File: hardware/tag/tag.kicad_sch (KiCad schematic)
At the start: 119 parts, among them J1 USB_C_Receptacle_USB2.0_16P, J10 Conn_01x02, J2 BATTERY, J3 BLE_Conn, J4 SOURCE, J5 STM SWD, J6 I2C, J7 UART, J8 BLE SWD, J9 AUX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

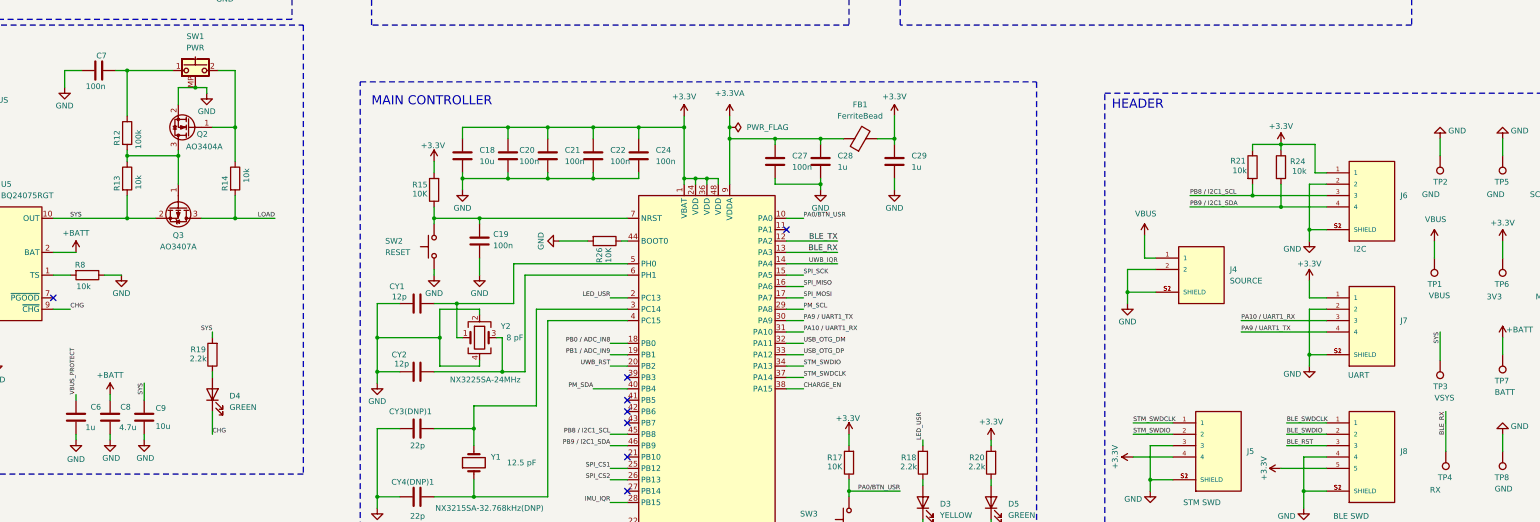
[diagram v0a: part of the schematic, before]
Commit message: update: add schottky diode to prevent the biased voltage back to soft latch circuit
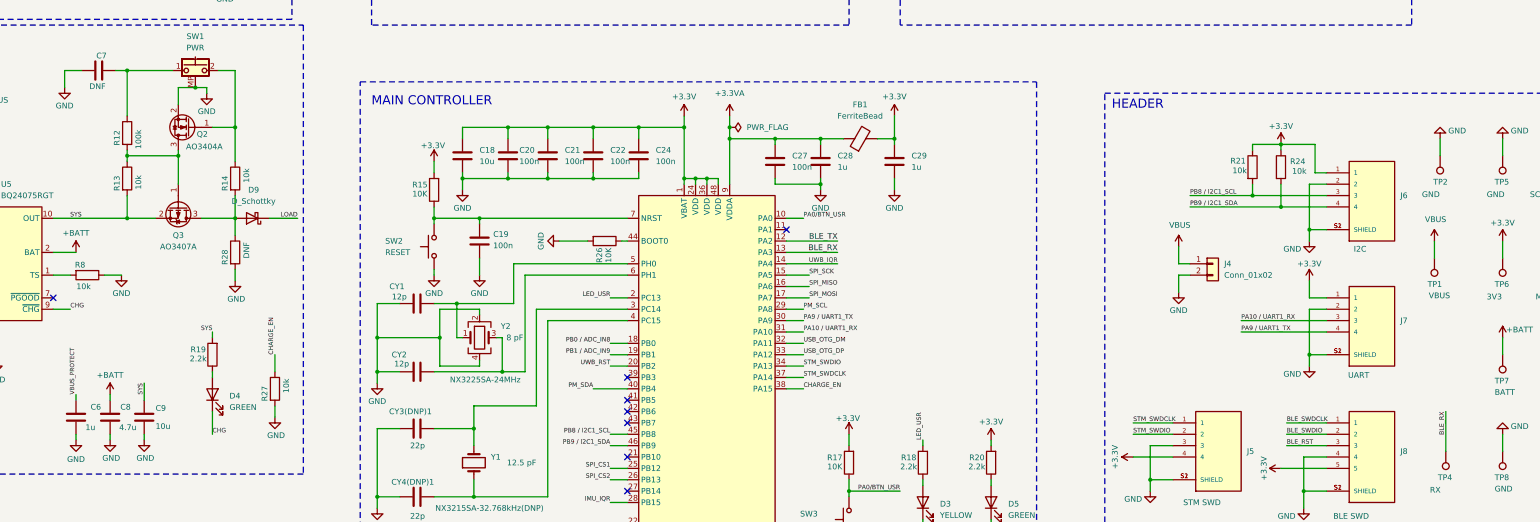
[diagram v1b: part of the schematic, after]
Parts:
- removed J4: SOURCE, Connector_JST:JST_PH_B2B-PH-K_1x02_P2.00mm_Vertical, symbol BM02B-SRSS-TB_LF__SN_:BM02B-SRSS-TB_LF__SN_
- removed TP3: VSYS, TestPoint:TestPoint_Pad_D1.5mm, symbol Connector:TestPoint
- added D9: D_Schottky, Diode_SMD:D_SOD-123, symbol Device:D_Schottky
- added J4: Conn_01x02, symbol Connector_Generic:Conn_01x02
- added R27: 10k, Resistor_SMD:R_0603_1608Metric, symbol Device:R
- added R28: DNF, Resistor_SMD:R_0603_1608Metric, symbol Device:R
- C1, C11, C12, C14, C2, C6, C8: footprint Capacitor_SMD:C_0805_2012Metric_Pad1.18x1.45mm_HandSolder -> Capacitor_SMD:C_0805_2012Metric
- C3, C4, C5: footprint Capacitor_SMD:C_0603_1608Metric_Pad1.08x0.95mm_HandSolder -> Capacitor_SMD:C_0603_1608Metric
- C7: value 100n -> DNF; footprint Capacitor_SMD:C_0603_1608Metric_Pad1.08x0.95mm_HandSolder -> Capacitor_SMD:C_0603_1608Metric
- R1, R11, R12, R13, R14, R19, R2, R5, R6, R8: footprint Resistor_SMD:R_0603_1608Metric_Pad0.98x0.95mm_HandSolder -> Resistor_SMD:R_0603_1608Metric
- TP10, TP11, TP12, TP13, TP14, TP15, TP4, TP9: footprint TestPoint:TestPoint_Pad_D1.5mm -> TestPoint:TestPoint_Pad_D1.0mm
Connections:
- net CHARGE_EN: now also R27.1
- net GND: now also J4.2 (Pin_2), R27.2, R28.2
- net LOAD: now also D9.1 (K); no longer Q3.3 (D), R14.2
- net VBUS: now also J4.1 (Pin_1)
- new net: D9.2 (A), Q3.3 (D), R14.2, R28.1

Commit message: wip hardware changes
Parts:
- C7: value DNF -> 100n(TBD)
- D8, D9: value D_Schottky -> MBR230LSFT1G
- J4: value Conn_01x02 -> EXT VBUS
- R28: value DNF -> 1k(TBD)
- R8: value 10k -> NTC 10k
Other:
- moved on the sheet: J4
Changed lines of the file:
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@@
 	(wire
 		(pts
-			(xy 360.68 185.42) (xy 358.14 185.42)
+			(xy 359.41 186.69) (xy 356.87 186.69)
 		)
 		(stroke
@@
 	(wire
 		(pts
-			(xy 358.14 187.96) (xy 358.14 191.77)
+			(xy 356.87 189.23) (xy 356.87 193.04)
 		)
 		(stroke
@@
 	(wire
 		(pts
-			(xy 360.68 187.96) (xy 358.14 187.96)
+			(xy 359.41 189.23) (xy 356.87 189.23)
 		)
 		(stroke
@@
 	(wire
 		(pts
-			(xy 358.14 185.42) (xy 358.14 181.61)
+			(xy 356.87 186.69) (xy 356.87 182.88)
 		)
 		(stroke
@@
 			)
 		)
-		(property "Value" "DNF"
-			(at 118.364 145.796 90)
+		(property "Value" "100n(TBD)"
+			(at 121.92 145.796 90)
 			(effects
 				(font
@@
 	(symbol
 		(lib_id "power:GND")
-		(at 358.14 191.77 0)
+		(at 356.87 193.04 0)
 		(mirror y)
 		(unit 1)
@@
 		(dnp no)
 		(property "Reference" "#PWR067"
-			(at 358.14 198.12 0)
+			(at 356.87 199.39 0)
 			(effects
 				(font
@@
 		)
 		(property "Value" "GND"
-			(at 358.14 195.834 0)
+			(at 356.87 197.104 0)
 			(effects
 				(font
@@
 		)
 		(property "Footprint" ""
-			(at 358.14 191.77 0)
+			(at 356.87 193.04 0)
 			(effects
 				(font
@@
 		)
 		(property "Datasheet" ""
-			(at 358.14 191.77 0)
+			(at 356.87 193.04 0)
 			(effects
 				(font
@@
 		)
 		(property "Description" "Power symbol creates a global label with name \"GND\" , ground"
-			(at 358.14 191.77 0)
+			(at 356.87 193.04 0)
 			(effects
 				(font
@@
 	(symbol
 		(lib_id "Connector_Generic:Conn_01x02")
-		(at 365.76 185.42 0)
+		(at 364.49 186.69 0)
 		(unit 1)
 		(exclude_from_sim no)
@@
 		(fields_autoplaced yes)
 		(property "Reference" "J4"
-			(at 368.3 185.4199 0)
+			(at 367.03 186.6899 0)
 			(effects
 				(font
@@
 			)
 		)
-		(property "Value" "Conn_01x02"
-			(at 368.3 187.9599 0)
+		(property "Value" "EXT VBUS"
+			(at 367.03 189.2299 0)
 			(effects
 				(font
@@
 		)
 		(property "Footprint" ""
-			(at 365.76 185.42 0)
+			(at 364.49 186.69 0)
 			(effects
 				(font
@@
 		)
 		(property "Datasheet" "~"
-			(at 365.76 185.42 0)
+			(at 364.49 186.69 0)
 			(effects
 				(font
@@
 		)
 		(property "Description" "Generic connector, single row, 01x02, script generated (kicad-library-utils/schlib/autogen/connector/)"
-			(at 365.76 185.42 0)
+			(at 364.49 186.69 0)
 			(effects
 				(font
@@
 	(symbol
 		(lib_id "power:VBUS")
-		(at 358.14 181.61 0)
+		(at 356.87 182.88 0)
 		(unit 1)
 		(exclude_from_sim no)
@@
 		(dnp no)
 		(property "Reference" "#PWR069"
-			(at 358.14 185.42 0)
+			(at 356.87 186.69 0)
 			(effects
 				(font
@@
 		)
 		(property "Value" "VBUS"
-			(at 358.394 176.784 0)
+			(at 357.124 178.054 0)
 			(effects
 				(font
@@
 		)
 		(property "Footprint" ""
-			(at 358.14 181.61 0)
+			(at 356.87 182.88 0)
 			(effects
 				(font
@@
 		)
 		(property "Datasheet" ""
-			(at 358.14 181.61 0)
+			(at 356.87 182.88 0)
 			(effects
 				(font
@@
 		)
 		(property "Description" "Power symbol creates a global label with name \"VBUS\""
-			(at 358.14 181.61 0)
+			(at 356.87 182.88 0)
 			(effects
 				(font
@@
 			)
 		)
-		(property "Value" "D_Schottky"
+		(property "Value" "MBR230LSFT1G"
 			(at 82.55 262.5724 90)
 			(effects
@@
 			)
 		)
-		(property "Value" "DNF"
-			(at 149.86 180.594 90)
+		(property "Value" "1k(TBD)"
+			(at 150.368 179.324 90)
 			(effects
 				(font
@@
 			)
 		)
-		(property "Value" "D_Schottky"
+		(property "Value" "MBR230LSFT1G"
 			(at 151.4475 171.45 0)
 			(effects
@@
 			)
 		)
-		(property "Value" "10k"
-			(at 115.062 190.5 90)
+		(property "Value" "NTC 10k"
+			(at 117.856 190.246 90)
 			(effects
 				(font

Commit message: Update: schematic with new dimensions and additional notes
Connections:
- net PWR_LATCH: now reaches Q2.1 (G), R14.1, SW1.2
- net PWR_LATCH: now also U7.39 (PB3)
- no-connect marks 34 -> 33
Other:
- note added: "NOTE: Use a 5 V-tolerant MCU GPIO. Configure the pin as open-drain."
- note added: "PWR_LATCH low = power off."
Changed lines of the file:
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@@
 	(rectangle
 		(start 17.78 132.08)
-		(end 162.56 232.41)
+		(end 173.99 232.41)
 		(stroke
 			(width 0)
@@
 		)
 	)
+	(text "NOTE: Use a 5 V-tolerant MCU GPIO.\n	  Configure the pin as open-drain.\n"
+		(exclude_from_sim no)
+		(at 147.574 158.496 0)
+		(effects
+			(font
+				(size 0.762 0.762)
+			)
+			(justify left)
+		)
+	)
 	(text "MAIN CONTROLLER"
 		(exclude_from_sim no)
@@
 		)
 	)
+	(text "PWR_LATCH low = power off."
+		(exclude_from_sim no)
+		(at 151.638 161.036 0)
+		(effects
+			(font
+				(size 0.762 0.762)
+			)
+			(justify left)
+		)
+	)
 	(text "HEADER"
 		(exclude_from_sim no)
@@
 	)
 	(no_connect
-		(at 234.95 210.82)
-	)
-	(no_connect
 		(at 207.01 60.96)
 	)
@@
 	(wire
 		(pts
+			(xy 147.32 154.94) (xy 153.67 154.94)
+		)
+		(stroke
+			(width 0)
+			(type default)
+		)
+	)
+	(wire
+		(pts
 			(xy 52.07 273.05) (xy 62.23 273.05)
 		)
@@
 	(wire
 		(pts
+			(xy 227.33 210.82) (xy 234.95 210.82)
+		)
+		(stroke
+			(width 0)
+			(type default)
+		)
+	)
+	(wire
+		(pts
 			(xy 207.01 201.93) (xy 205.74 201.93)
 		)
@@
 		)
 	)
+	(label "PWR_LATCH"
+		(at 227.33 210.82 180)
+		(effects
+			(font
+				(size 1 1)
+			)
+			(justify right bottom)
+		)
+	)
 	(label "SPI_SCK"
 		(at 275.59 187.96 0)
@@
 		)
 	)
+	(label "PWR_LATCH"
+		(at 153.67 154.94 0)
+		(effects
+			(font
+				(size 1 1)
+			)
+			(justify left bottom)
+		)
+	)
